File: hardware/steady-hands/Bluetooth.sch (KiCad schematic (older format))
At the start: 4 parts, among them J4 ARM_SWD, U5 BGM13S

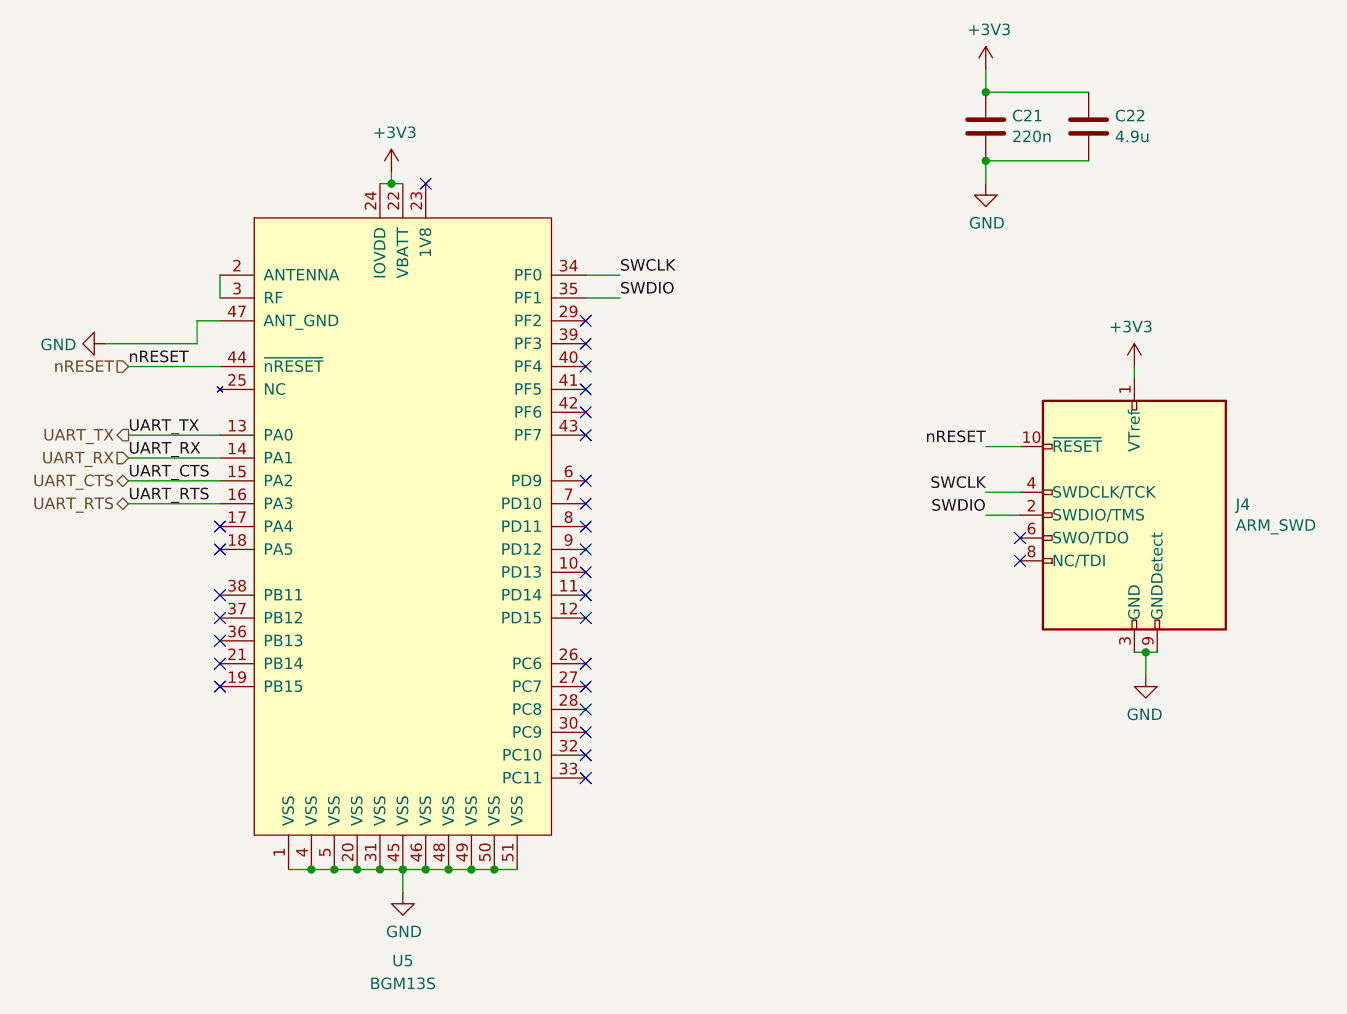
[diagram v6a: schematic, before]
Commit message: Edits PCB layout
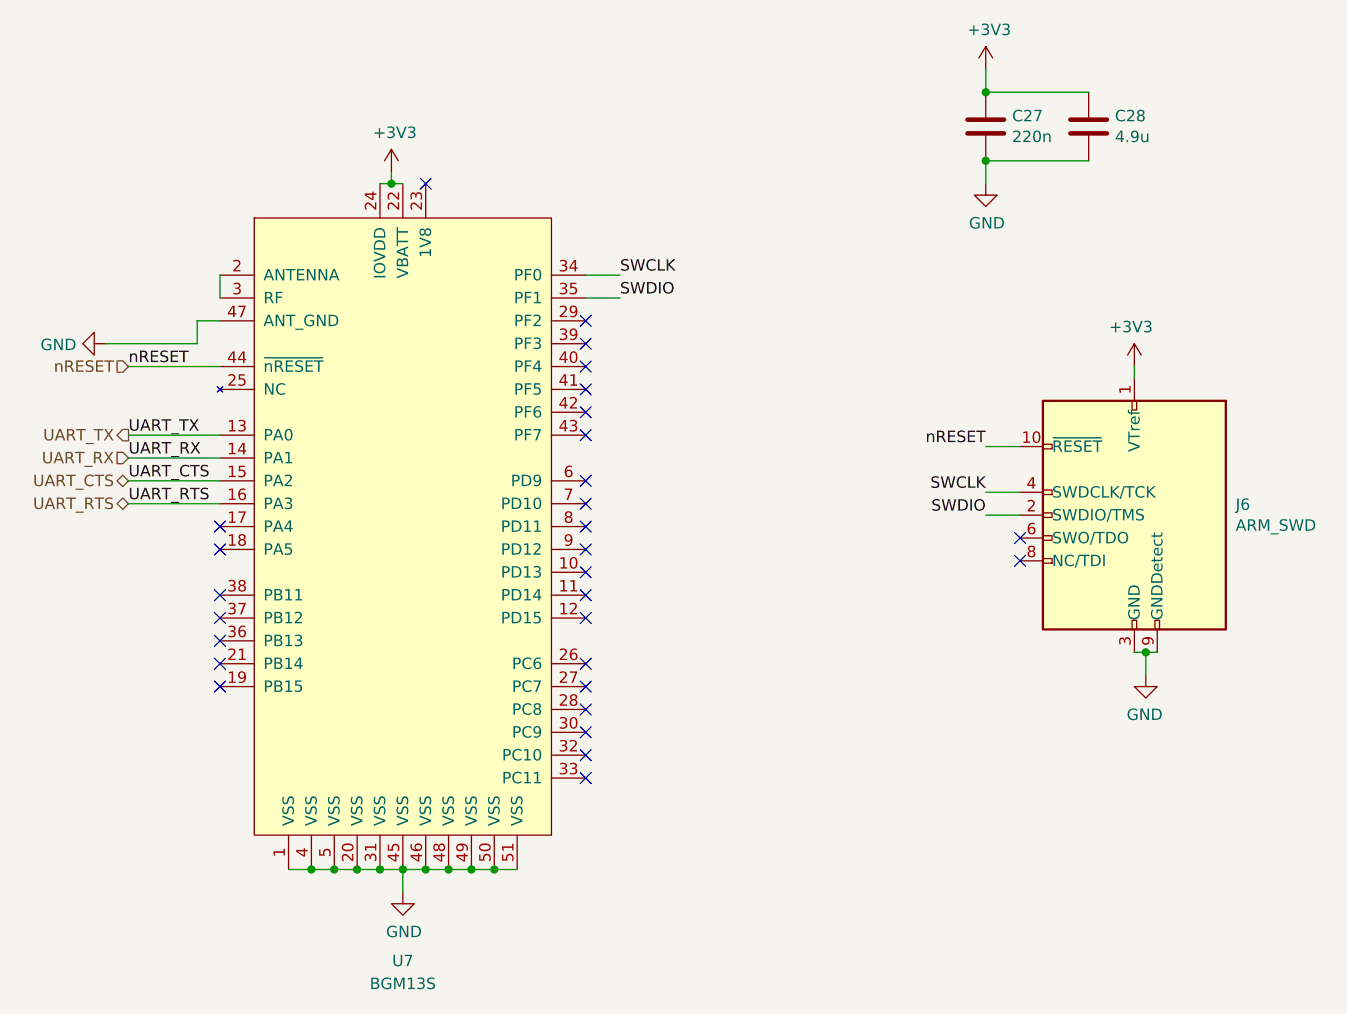
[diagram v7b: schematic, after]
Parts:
- J6: renamed from J4; footprint Sij_Connectors:FTSH-105-01-X-DV -> Sij_Connectors:FTSH-105-01-L-DV-K
- renumbered C21 to C27, C22 to C28, U5 to U7
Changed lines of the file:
@@
 P 5800 3650
 AR Path="/5EF78FC7" Ref="U?"  Part="1"
-AR Path="/5EF722F6/5EF78FC7" Ref="U5"  Part="1"
-F 0 "U5" H 5800 1850 50  0000 C CNN
+AR Path="/5EF722F6/5EF78FC7" Ref="U7"  Part="1"
+F 0 "U7" H 5800 1850 50  0000 C CNN
 F 1 "BGM13S" H 5800 1750 50  0000 C CNN
 F 2 "Sij_MCU:BGM13S" H 5800 3800 50  0001 C CNN
@@
 	4900 2750 4500 2750
 $Comp
-L power:GND #PWR0137
+L power:GND #PWR056
 U 1 1 5EFC41D5
 P 4500 2750
-F 0 "#PWR0137" H 4500 2500 50  0001 C CNN
+F 0 "#PWR056" H 4500 2500 50  0001 C CNN
 F 1 "GND" V 4505 2622 50  0000 R CNN
 F 2 "" H 4500 2750 50  0001 C CNN
@@
 	5800 5050 5800 5150
 $Comp
-L power:GND #PWR0138
+L power:GND #PWR058
 U 1 1 5EFC4D28
 P 5800 5150
-F 0 "#PWR0138" H 5800 4900 50  0001 C CNN
+F 0 "#PWR058" H 5800 4900 50  0001 C CNN
 F 1 "GND" H 5805 4977 50  0000 C CNN
 F 2 "" H 5800 5150 50  0001 C CNN
@@
 $EndComp
 $Comp
-L Connector:Conn_ARM_JTAG_SWD_10 J4
+L Connector:Conn_ARM_JTAG_SWD_10 J6
 U 1 1 5F142B1F
 P 9000 3500
-F 0 "J4" H 8557 3546 50  0000 R CNN
+F 0 "J6" H 8557 3546 50  0000 R CNN
 F 1 "ARM_SWD" H 8557 3455 50  0000 R CNN
-F 2 "Sij_Connectors:FTSH-105-01-X-DV" H 9000 3500 50  0001 C CNN
+F 2 "Sij_Connectors:FTSH-105-01-L-DV-K" H 9000 3500 50  0001 C CNN
 F 3 "http://infocenter.arm.com/help/topic/com.arm.doc.ddi0314h/DDI0314H_coresight_components_trm.pdf" V 8650 2250 50  0001 C CNN
 	1    9000 3500
@@
 NoConn ~ 8500 3600
 $Comp
-L power:+3V3 #PWR0139
+L power:+3V3 #PWR061
 U 1 1 5F1483CA
 P 9000 2850
-F 0 "#PWR0139" H 9000 2700 50  0001 C CNN
+F 0 "#PWR061" H 9000 2700 50  0001 C CNN
 F 1 "+3V3" H 9015 3023 50  0000 C CNN
 F 2 "" H 9000 2850 50  0001 C CNN
@@
 $EndComp
 $Comp
-L power:GND #PWR0140
+L power:GND #PWR062
 U 1 1 5F14849D
 P 9050 4200
-F 0 "#PWR0140" H 9050 3950 50  0001 C CNN
+F 0 "#PWR062" H 9050 3950 50  0001 C CNN
 F 1 "GND" H 9055 4027 50  0000 C CNN
 F 2 "" H 9050 4200 50  0001 C CNN
@@
 	5750 2050 5800 2050
 $Comp
-L power:+3V3 #PWR0141
+L power:+3V3 #PWR057
 U 1 1 5F155003
 P 5750 2000
-F 0 "#PWR0141" H 5750 1850 50  0001 C CNN
+F 0 "#PWR057" H 5750 1850 50  0001 C CNN
 F 1 "+3V3" H 5765 2173 50  0000 C CNN
 F 2 "" H 5750 2000 50  0001 C CNN
@@
 NoConn ~ 5900 2050
 $Comp
-L Device:C C21
+L Device:C C27
 U 1 1 5F156DBD
 P 8350 1800
-F 0 "C21" H 8465 1846 50  0000 L CNN
+F 0 "C27" H 8465 1846 50  0000 L CNN
 F 1 "220n" H 8465 1755 50  0000 L CNN
 F 2 "Capacitor_SMD:C_0402_1005Metric" H 8388 1650 50  0001 C CNN
@@
 $EndComp
 $Comp
-L Device:C C22
+L Device:C C28
 U 1 1 5F1574B3
 P 8800 1800
-F 0 "C22" H 8915 1846 50  0000 L CNN
+F 0 "C28" H 8915 1846 50  0000 L CNN
 F 1 "4.9u" H 8915 1755 50  0000 L CNN
 F 2 "Capacitor_SMD:C_0402_1005Metric" H 8838 1650 50  0001 C CNN
@@
 Connection ~ 8350 1950
 $Comp
-L power:+3V3 #PWR0142
+L power:+3V3 #PWR059
 U 1 1 5F15A77D
 P 8350 1550
-F 0 "#PWR0142" H 8350 1400 50  0001 C CNN
+F 0 "#PWR059" H 8350 1400 50  0001 C CNN
 F 1 "+3V3" H 8365 1723 50  0000 C CNN
 F 2 "" H 8350 1550 50  0001 C CNN
@@
 $EndComp
 $Comp
-L power:GND #PWR0143
+L power:GND #PWR060
 U 1 1 5F15AB86
 P 8350 2050
-F 0 "#PWR0143" H 8350 1800 50  0001 C CNN
+F 0 "#PWR060" H 8350 1800 50  0001 C CNN
 F 1 "GND" H 8355 1877 50  0000 C CNN
 F 2 "" H 8350 2050 50  0001 C CNN
